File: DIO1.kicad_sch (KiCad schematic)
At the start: 25 parts, among them J10 音声入力, J11 音声出力, J3 カフＳＷ１, J4 カフＳＷ２, J5 カフＳＷ３, J6 カフＳＷ４, J7 カフＳＷ５, J8 DI-1, J9 DO-1, K1 G6A-274P-ST-US DC12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

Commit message: カフコントローラ
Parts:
- removed H1, H2, H3, H4: MountingHole, MountingHole:MountingHole_3.2mm_M3, symbol Mechanical:MountingHole
- added J18: Out, Connector_PinHeader_2.54mm:PinHeader_1x02_P2.54mm_Vertical, symbol Connector_Generic:Conn_01x02
- added J19: In, Connector_PinHeader_2.54mm:PinHeader_1x03_P2.54mm_Vertical, symbol Connector_Generic:Conn_01x03
- J10: value 音声入力 -> AUDIO_IN; footprint Connector_PinHeader_1.27mm:PinHeader_1x06_P1.27mm_Vertical -> Connector_PinHeader_2.54mm:PinHeader_1x06_P2.54mm_Vertical
- J11: value 音声出力 -> AUDIO_OUT; footprint Connector_PinHeader_1.27mm:PinHeader_1x06_P1.27mm_Vertical -> Connector_PinHeader_2.54mm:PinHeader_1x06_P2.54mm_Vertical
- J3: value カフＳＷ１ -> SW1; footprint Connector_PinHeader_1.27mm:PinHeader_1x04_P1.27mm_Vertical -> Connector_PinHeader_2.54mm:PinHeader_1x04_P2.54mm_Vertical
- J4: value カフＳＷ２ -> SW2; footprint Connector_PinHeader_1.27mm:PinHeader_1x04_P1.27mm_Vertical -> Connector_PinHeader_2.54mm:PinHeader_1x04_P2.54mm_Vertical
- J5: value カフＳＷ３ -> SW3; footprint Connector_PinHeader_1.27mm:PinHeader_1x04_P1.27mm_Vertical -> Connector_PinHeader_2.54mm:PinHeader_1x04_P2.54mm_Vertical
- J6: value カフＳＷ４ -> SW4; footprint Connector_PinHeader_1.27mm:PinHeader_1x04_P1.27mm_Vertical -> Connector_PinHeader_2.54mm:PinHeader_1x04_P2.54mm_Vertical
- J7: value カフＳＷ５ -> SW5; footprint Connector_PinHeader_1.27mm:PinHeader_1x04_P1.27mm_Vertical -> Connector_PinHeader_2.54mm:PinHeader_1x04_P2.54mm_Vertical
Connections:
- net +5V: no longer J8.10 (Pin_10), J9.10 (Pin_10)
- net GND: no longer J9.9 (Pin_9)
- net at J8.1 (Pin_1): now also J19.3 (Pin_3)
- net at J8.2 (Pin_2): now also J19.2 (Pin_2)
- net at J8.3 (Pin_3): now also J19.1 (Pin_1)
- net at J9.2 (Pin_2): now also J18.2 (Pin_2)
- net at J9.3 (Pin_3): now also J18.1 (Pin_1)
- new net COM0: J8.10 (Pin_10)
- new net MCOM1: J9.9 (Pin_9)
- new net PCOM1: J9.10 (Pin_10)
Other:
- moved on the sheet: J3

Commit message: コネクタをピンヘッダに変更
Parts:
- J8, J9: footprint Connector_Phoenix_MC:PhoenixContact_MC_1,5_10-G-3.81_1x10_P3.81mm_Horizontal -> Connector_PinHeader_2.54mm:PinHeader_1x10_P2.54mm_Vertical
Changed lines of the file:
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@@
       (effects (font (size 1.27 1.27)) (justify left))
     )
-    (property "Footprint" "Connector_Phoenix_MC:PhoenixContact_MC_1,5_10-G-3.81_1x10_P3.81mm_Horizontal" (at 120.65 40.64 0)
+    (property "Footprint" "Connector_PinHeader_2.54mm:PinHeader_1x10_P2.54mm_Vertical" (at 120.65 40.64 0)
       (effects (font (size 1.27 1.27)) hide)
     )
@@
       (effects (font (size 1.27 1.27)) (justify left))
     )
-    (property "Footprint" "Connector_Phoenix_MC:PhoenixContact_MC_1,5_10-G-3.81_1x10_P3.81mm_Horizontal" (at 120.65 72.39 0)
-      (effects (font (size 1.27 1.27)) hide)
-    )
+    (property "Footprint" "Connector_PinHeader_2.54mm:PinHeader_1x10_P2.54mm_Vertical" (at 120.65 72.39 0)
+      (effects (font (size 1.27 1.27)) hide)
+    )

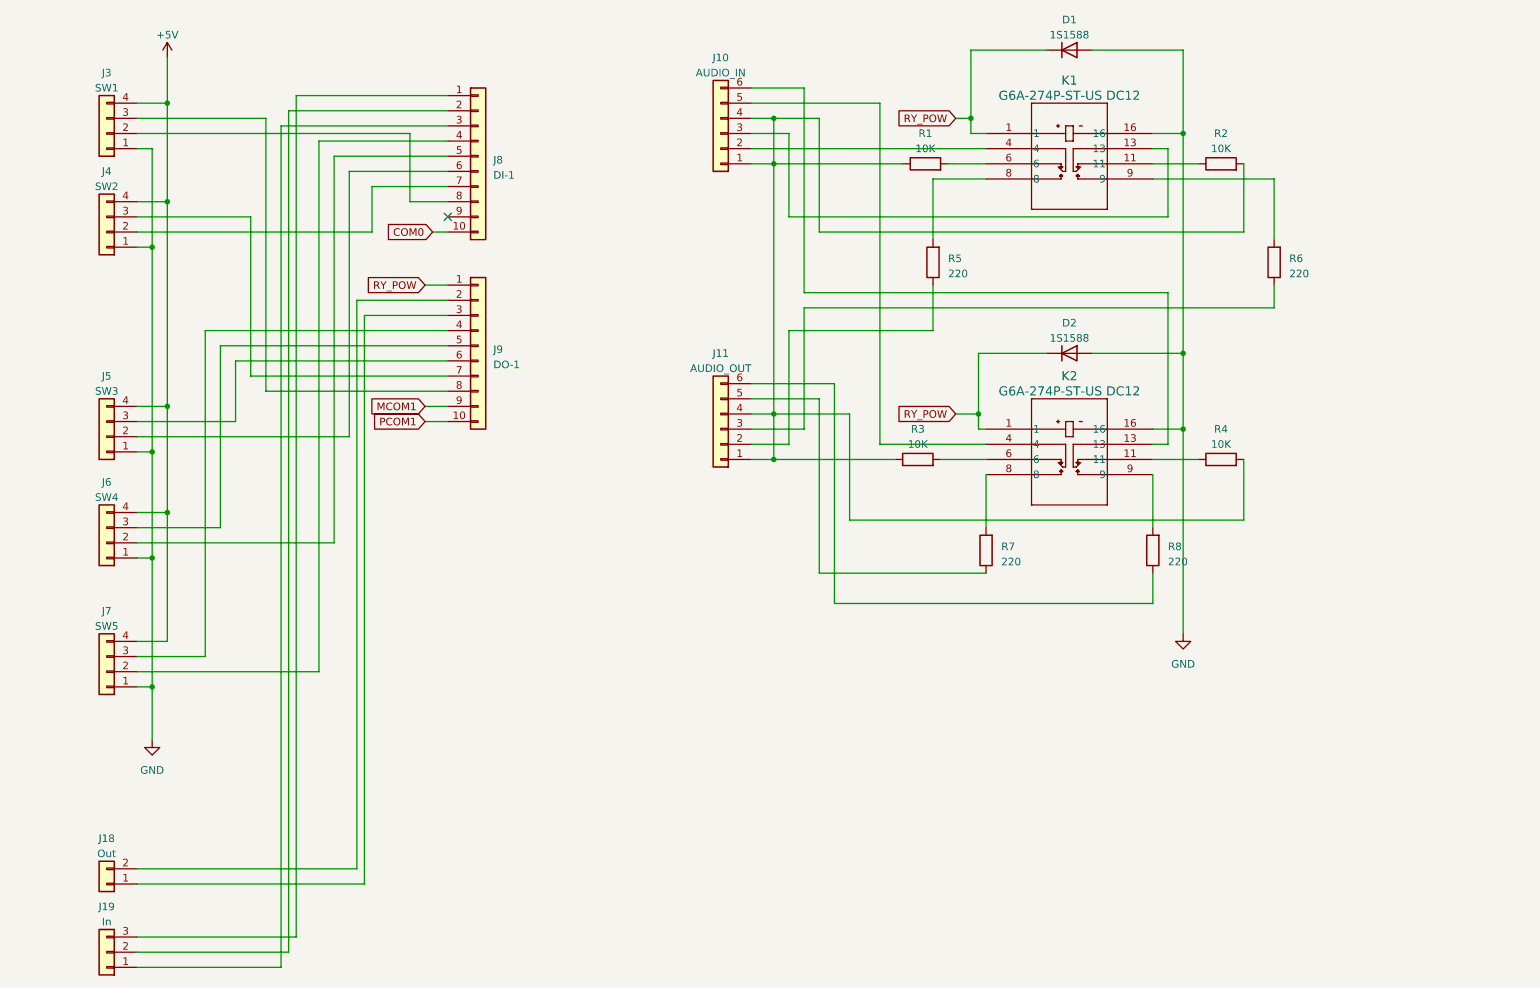
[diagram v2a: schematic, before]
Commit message: 端子をピンヘッダ2x10に変更
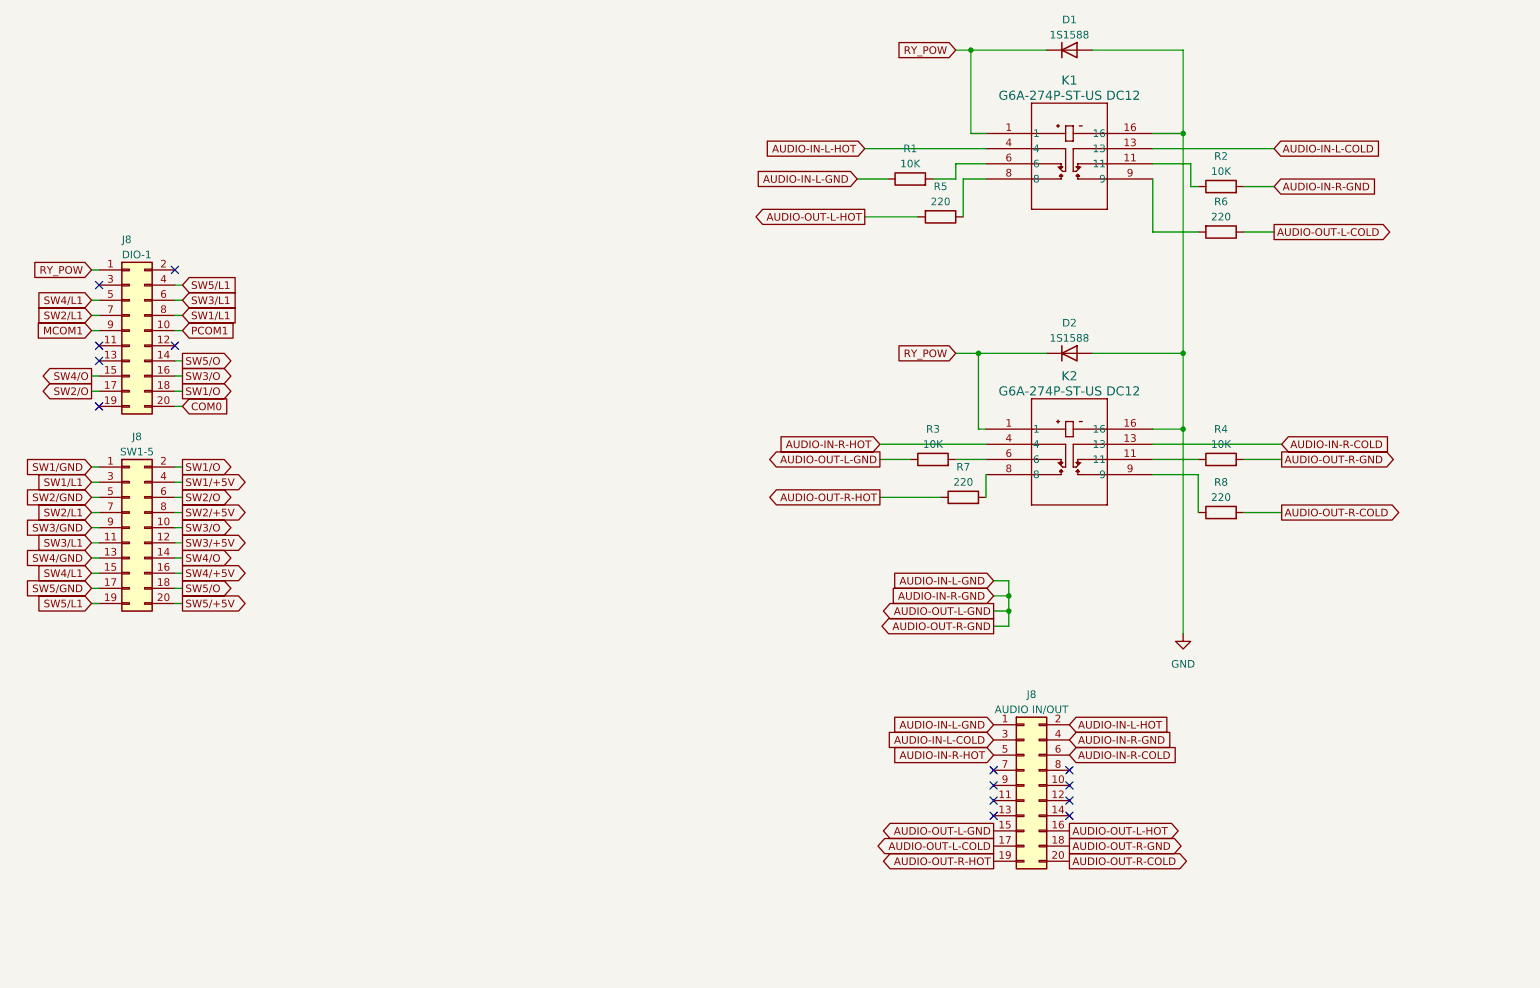
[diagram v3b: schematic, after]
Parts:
- removed J10: AUDIO_IN, Connector_PinHeader_2.54mm:PinHeader_1x06_P2.54mm_Vertical, symbol Connector_Generic:Conn_01x06
- removed J11: AUDIO_OUT, Connector_PinHeader_2.54mm:PinHeader_1x06_P2.54mm_Vertical, symbol Connector_Generic:Conn_01x06
- removed J18: Out, Connector_PinHeader_2.54mm:PinHeader_1x02_P2.54mm_Vertical, symbol Connector_Generic:Conn_01x02
- removed J19: In, Connector_PinHeader_2.54mm:PinHeader_1x03_P2.54mm_Vertical, symbol Connector_Generic:Conn_01x03
- removed J3: SW1, Connector_PinHeader_2.54mm:PinHeader_1x04_P2.54mm_Vertical, symbol Connector_Generic:Conn_01x04
- removed J4: SW2, Connector_PinHeader_2.54mm:PinHeader_1x04_P2.54mm_Vertical, symbol Connector_Generic:Conn_01x04
- removed J5: SW3, Connector_PinHeader_2.54mm:PinHeader_1x04_P2.54mm_Vertical, symbol Connector_Generic:Conn_01x04
- removed J6: SW4, Connector_PinHeader_2.54mm:PinHeader_1x04_P2.54mm_Vertical, symbol Connector_Generic:Conn_01x04
- removed J7: SW5, Connector_PinHeader_2.54mm:PinHeader_1x04_P2.54mm_Vertical, symbol Connector_Generic:Conn_01x04
- removed J9: DO-1, Connector_PinHeader_2.54mm:PinHeader_1x10_P2.54mm_Vertical, symbol Connector_Generic:Conn_01x10
- added J8: AUDIO IN/OUT, Connector_PinHeader_2.54mm:PinHeader_2x10_P2.54mm_Vertical, symbol Connector_Generic:Conn_02x10_Odd_Even
- added J8: SW1-5, Connector_PinHeader_2.54mm:PinHeader_2x10_P2.54mm_Vertical, symbol Connector_Generic:Conn_02x10_Odd_Even
- J8: value DI-1 -> DIO-1; footprint Connector_PinHeader_2.54mm:PinHeader_1x10_P2.54mm_Vertical -> Connector_PinHeader_2.54mm:PinHeader_2x10_P2.54mm_Vertical; symbol Connector_Generic:Conn_01x10 -> Connector_Generic:Conn_02x10_Odd_Even
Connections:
- net COM0: now also J8.20 (Pin_20); no longer J8.10 (Pin_10)
- net MCOM1: now also J8.9 (Pin_9)
- net PCOM1: now also J8.10 (Pin_10)
- net RY_POW: now also J8.1 (Pin_1)
- net AUDIO-IN-L-GND: now reaches R1.1, R2.2, R3.1, R4.2
- net AUDIO-IN-L-GND: now also J8.1 (Pin_1), J8.15 (Pin_15), J8.18 (Pin_18), J8.4 (Pin_4)
- net AUDIO-OUT-R-HOT: now reaches R7.1
- net AUDIO-OUT-R-HOT: now also J8.19 (Pin_19)
- net AUDIO-IN-R-COLD: now reaches K2.13
- net AUDIO-IN-R-COLD: now also J8.6 (Pin_6)
- net AUDIO-IN-R-HOT: now reaches K2.4
- net AUDIO-IN-R-HOT: now also J8.5 (Pin_5)
- net at K2.9: now also R8.1; no longer R8.2
- net SW5/L1: now reaches J8.4 (Pin_4)
- net SW5/L1: now also J8.19 (Pin_19)
- net AUDIO-IN-L-HOT: now reaches K1.4
- net AUDIO-IN-L-HOT: now also J8.2 (Pin_2)
- net AUDIO-IN-L-COLD: now reaches K1.13
- net AUDIO-IN-L-COLD: now also J8.3 (Pin_3)
- net at R5.1: now also K1.8
- net AUDIO-OUT-L-COLD: now reaches R6.1
- net AUDIO-OUT-L-COLD: now also J8.17 (Pin_17)
- net SW4/L1: now reaches J8.5 (Pin_5)
- net SW4/L1: now also J8.15 (Pin_15)
- net SW3/L1: now reaches J8.6 (Pin_6)
- net SW3/L1: now also J8.11 (Pin_11)
- net SW2/L1: now reaches J8.7 (Pin_7)
- net SW2/L1: now also J8.7 (Pin_7)
- net SW1/L1: now reaches J8.8 (Pin_8)
- net SW1/L1: now also J8.3 (Pin_3)
- net AUDIO-OUT-L-HOT: now reaches R5.2
- net AUDIO-OUT-L-HOT: now also J8.16 (Pin_16); no longer K1.8
- new net AUDIO-OUT-R-COLD: J8.20 (Pin_20), R8.2
- new net SW1/+5V: J8.4 (Pin_4)
- new net SW1/GND: J8.1 (Pin_1)
- new net SW1/O: J8.18 (Pin_18), J8.2 (Pin_2)
- new net SW2/+5V: J8.8 (Pin_8)
- new net SW2/GND: J8.5 (Pin_5)
- new net SW2/O: J8.17 (Pin_17), J8.6 (Pin_6)
- new net SW3/+5V: J8.12 (Pin_12)
- new net SW3/GND: J8.9 (Pin_9)
- new net SW3/O: J8.10 (Pin_10), J8.16 (Pin_16)
- new net SW4/+5V: J8.16 (Pin_16)
- new net SW4/GND: J8.13 (Pin_13)
- new net SW4/O: J8.14 (Pin_14), J8.15 (Pin_15)
- new net SW5/+5V: J8.20 (Pin_20)
- new net SW5/GND: J8.17 (Pin_17)
- new net SW5/O: J8.14 (Pin_14), J8.18 (Pin_18)
- no-connect marks 1 -> 14
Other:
- moved on the sheet: R1, R2, R3, R5, R6, R7, R8

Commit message: リレー ロジックミス修正
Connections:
- net GND is gone; now on net RY_POW: D1.2 (A), D2.2 (A), K1.16, K2.16
- net PCOM1: now also D1.1 (K), D2.1 (K), K1.1, K2.1
- net RY_POW: no longer D1.1 (K), D2.1 (K), K1.1, K2.1
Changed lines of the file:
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@@
 (kicad_sch (version 20230121) (generator eeschema)
   (paper "A4")
-  (junction (at 238.76 86.36) (diameter 0) (color 0 0 0 0)
+  (junction (at 203.2 22.86) (diameter 0) (color 0 0 0 0)
+  )
+  (junction (at 209.55 116.84) (diameter 0) (color 0 0 0 0)
+  )
+  (junction (at 238.76 22.86) (diameter 0) (color 0 0 0 0)
   )
   (junction (at 204.47 73.66) (diameter 0) (color 0 0 0 0)
   )
-  (junction (at 209.55 116.84) (diameter 0) (color 0 0 0 0)
-  )
-  (junction (at 238.76 36.83) (diameter 0) (color 0 0 0 0)
-  )
   (junction (at 238.76 73.66) (diameter 0) (color 0 0 0 0)
   )
   (junction (at 209.55 114.3) (diameter 0) (color 0 0 0 0)
-  )
-  (junction (at 203.2 22.86) (diameter 0) (color 0 0 0 0)
   )
   (no_connect (at 57.15 74.93))
@@
     (stroke (width 0) (type default))
   )
-  (wire (pts (xy 200.66 73.66) (xy 204.47 73.66))
-    (stroke (width 0) (type default))
-  )
   (wire (pts (xy 201.93 44.45) (xy 205.74 44.45))
     (stroke (width 0) (type default))
@@
     (stroke (width 0) (type default))
   )
-  (wire (pts (xy 203.2 22.86) (xy 200.66 22.86))
-    (stroke (width 0) (type default))
-  )
   (wire (pts (xy 233.68 86.36) (xy 238.76 86.36))
     (stroke (width 0) (type default))
@@
     (stroke (width 0) (type default))
   )
+  (wire (pts (xy 238.76 22.86) (xy 243.84 22.86))
+    (stroke (width 0) (type default))
+  )
   (wire (pts (xy 248.92 53.34) (xy 254 53.34))
     (stroke (width 0) (type default))
   )
-  (wire (pts (xy 238.76 36.83) (xy 238.76 73.66))
+  (wire (pts (xy 198.12 22.86) (xy 203.2 22.86))
     (stroke (width 0) (type default))
   )
@@
     (stroke (width 0) (type default))
   )
+  (wire (pts (xy 199.39 73.66) (xy 204.47 73.66))
+    (stroke (width 0) (type default))
+  )
   (wire (pts (xy 55.88 80.01) (xy 57.15 80.01))
     (stroke (width 0) (type default))
@@
     (stroke (width 0) (type default))
   )
-  (wire (pts (xy 238.76 86.36) (xy 238.76 120.65))
-    (stroke (width 0) (type default))
-  )
   (wire (pts (xy 215.9 22.86) (xy 203.2 22.86))
     (stroke (width 0) (type default))
@@
     (stroke (width 0) (type default))
   )
+  (wire (pts (xy 238.76 73.66) (xy 243.84 73.66))
+    (stroke (width 0) (type default))
+  )
   (wire (pts (xy 185.42 39.37) (xy 205.74 39.37))
     (stroke (width 0) (type default))
@@
     )
   )
+  (global_label "PCOM1" (shape input) (at 198.12 22.86 180) (fields_autoplaced)
+    (effects (font (size 1.27 1.27)) (justify right))
+    (property "Intersheetrefs" "${INTERSHEET_REFS}" (at 188.6828 22.86 0)
+      (effects (font (size 1.27 1.27)) (justify right) hide)
+    )
+  )
   (global_label "SW2{slash}O" (shape output) (at 71.12 97.79 0) (fields_autoplaced)
     (effects (font (size 1.27 1.27)) (justify left))
@@
     )
   )
-  (global_label "RY_POW" (shape input) (at 200.66 22.86 180) (fields_autoplaced)
-    (effects (font (size 1.27 1.27)) (justify right))
-    (property "Intersheetrefs" "${INTERSHEET_REFS}" (at 190.3761 22.86 0)
-      (effects (font (size 1.27 1.27)) (justify right) hide)
+  (global_label "RY_POW" (shape input) (at 243.84 22.86 0) (fields_autoplaced)
+    (effects (font (size 1.27 1.27)) (justify left))
+    (property "Intersheetrefs" "${INTERSHEET_REFS}" (at 254.1239 22.86 0)
+      (effects (font (size 1.27 1.27)) (justify left) hide)
     )
   )
@@
     )
   )
-  (global_label "RY_POW" (shape input) (at 200.66 73.66 180) (fields_autoplaced)
-    (effects (font (size 1.27 1.27)) (justify right))
-    (property "Intersheetrefs" "${INTERSHEET_REFS}" (at 190.3761 73.66 0)
-      (effects (font (size 1.27 1.27)) (justify right) hide)
-    )
-  )
   (global_label "SW5{slash}L1" (shape input) (at 71.12 62.23 0) (fields_autoplaced)
     (effects (font (size 1.27 1.27)) (justify left))
@@
     )
   )
+  (global_label "RY_POW" (shape input) (at 243.84 73.66 0) (fields_autoplaced)
+    (effects (font (size 1.27 1.27)) (justify left))
+    (property "Intersheetrefs" "${INTERSHEET_REFS}" (at 254.1239 73.66 0)
+      (effects (font (size 1.27 1.27)) (justify left) hide)
+    )
+  )
   (global_label "SW1{slash}GND" (shape input) (at 55.88 92.71 180) (fields_autoplaced)
     (effects (font (size 1.27 1.27)) (justify right))
@@
     (effects (font (size 1.27 1.27)) (justify right))
     (property "Intersheetrefs" "${INTERSHEET_REFS}" (at 43.9028 107.95 0)
+      (effects (font (size 1.27 1.27)) (justify right) hide)
+    )
+  )
+  (global_label "PCOM1" (shape input) (at 199.39 73.66 180) (fields_autoplaced)
+    (effects (font (size 1.27 1.27)) (justify right))
+    (property "Intersheetrefs" "${INTERSHEET_REFS}" (at 189.9528 73.66 0)
       (effects (font (size 1.27 1.27)) (justify right) hide)
     )
@@
         )
       )
-    )
-  )
-  (symbol (lib_id "power:GND") (at 238.76 120.65 0) (unit 1)
-    (in_bom yes) (on_board yes) (dnp no) (fields_autoplaced)
-    (property "Reference" "#PWR09" (at 238.76 127 0)
-      (effects (font (size 1.27 1.27)) hide)
-    )
-    (property "Value" "GND" (at 238.76 125.73 0)
-      (effects (font (size 1.27 1.27)))
-    )
-    (property "Footprint" "" (at 238.76 120.65 0)
-      (effects (font (size 1.27 1.27)) hide)
-    )
-    (property "Datasheet" "" (at 238.76 120.65 0)
-      (effects (font (size 1.27 1.27)) hide)
-    )
-    (pin "1")
-    (instances
-      (project "CoughController"
-        (path "/6320cb9c-a8f8-4921-856c-dd9ecac4c251"
-          (reference "#PWR09") (unit 1)
-        )
-        (path "/6320cb9c-a8f8-4921-856c-dd9ecac4c251/2e422247-f02f-4cb3-84b7-f23c5e92f071"
-          (reference "#PWR015") (unit 1)
-        )
-      )
